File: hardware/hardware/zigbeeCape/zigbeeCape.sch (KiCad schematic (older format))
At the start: 46 parts, among them J1 Conn_ARM_JTAG_SWD_10, SW1 SW_MEC_5E, SW2 SW_MEC_5E, SW3 SW_MEC_5E, SW4 SW_MEC_5E, SW5 SW_MEC_5E, U1 CC1352R, Y1 32.768kHz, Y2 48MHz

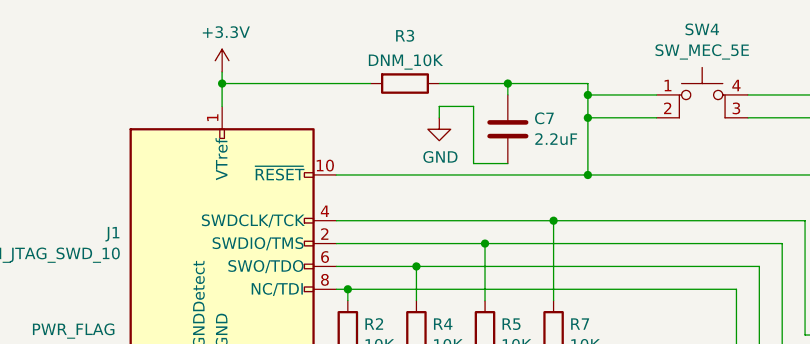
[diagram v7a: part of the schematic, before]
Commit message: Updated BOM, small changes to PCB and schematic
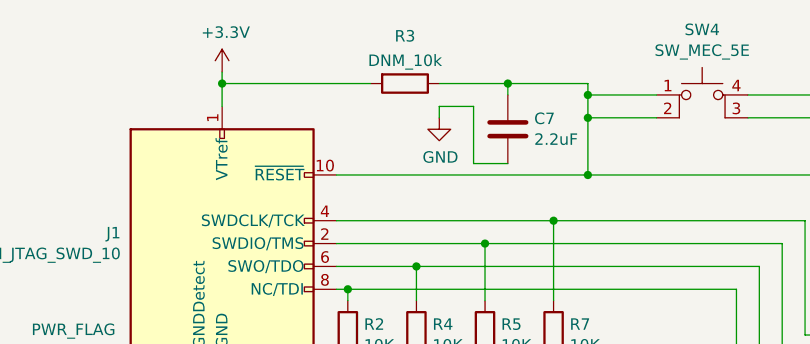
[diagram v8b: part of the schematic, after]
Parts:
- C12, C14: footprint Capacitor_SMD:C_0603_1608Metric_Pad1.08x0.95mm_HandSolder -> Capacitor_SMD:C_0402_1005Metric_Pad0.74x0.62mm_HandSolder
- R3: value DNM_10K -> DNM_10k
